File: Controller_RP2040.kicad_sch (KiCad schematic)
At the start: 11 parts, among them J2 Conn_ARM_SWD_TagConnect_TC203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, U3 NCP1117-3.3

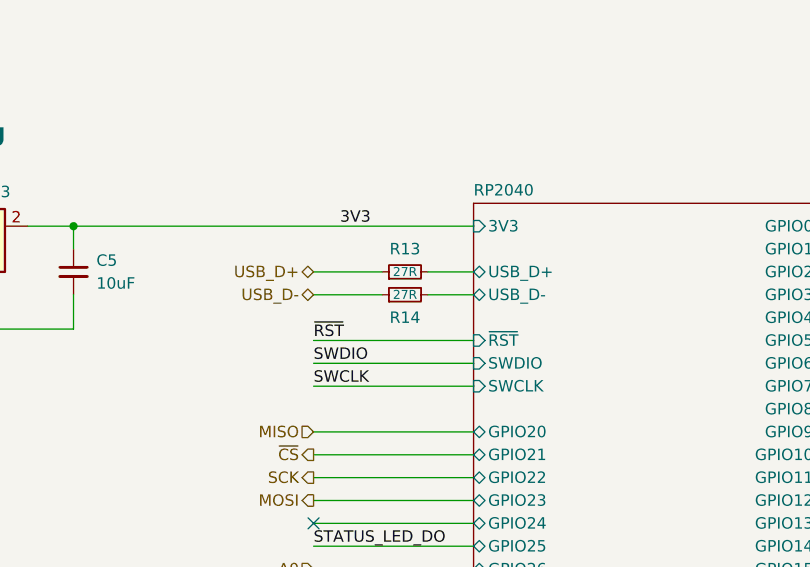
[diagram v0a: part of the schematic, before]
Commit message: Update usb data pins, update to fix 3v3 reg not adj
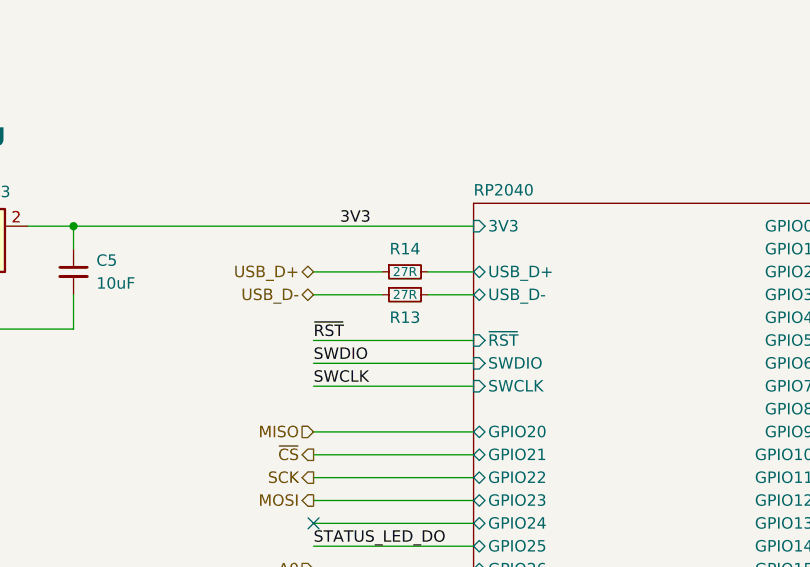
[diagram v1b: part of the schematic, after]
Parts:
- U3: LCSC C233236 -> C146799; MPN NCP1117LPSTADT3G -> NCP1117LPST33T3G; Supplier PN NCP1117LPSTADT3GOSCT-ND -> NCP1117LPST33T3GOSCT-ND
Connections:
- net RP2040/USB_D+: now also R14.2; no longer R13.2
- net RP2040/USB_D-: now also R13.2; no longer R14.2
- net USB_D+: now also R14.1; no longer R13.1
- net USB_D-: now also R13.1; no longer R14.1
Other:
- moved on the sheet: R13, R14
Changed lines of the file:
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@@
 	(symbol
 		(lib_id "Device:R_Small")
-		(at 107.95 67.31 90)
+		(at 107.95 64.77 90)
+		(mirror x)
 		(unit 1)
 		(exclude_from_sim no)
@@
 		(dnp no)
 		(property "Reference" "R14"
-			(at 107.95 69.85 90)
+			(at 107.95 62.23 90)
 			(effects
 				(font
@@
 		)
 		(property "Value" "27R"
-			(at 107.95 67.31 90)
+			(at 107.95 64.77 90)
 			(effects
 				(font
@@
 		)
 		(property "Footprint" "Resistor_SMD:R_0402_1005Metric"
-			(at 107.95 67.31 0)
+			(at 107.95 64.77 0)
 			(effects
 				(font
@@
 		)
 		(property "Datasheet" "https://www.yageo.com/upload/media/product/products/datasheet/rchip/PYu-RC_Group_51_RoHS_L_12.pdf"
-			(at 107.95 67.31 0)
+			(at 107.95 64.77 0)
 			(effects
 				(font
@@
 		)
 		(property "Description" "27 Ohms ±1% 0.063W, 1/16W Chip Resistor 0402 (1005 Metric) Moisture Resistant Thick Film"
-			(at 107.95 67.31 0)
+			(at 107.95 64.77 0)
 			(effects
 				(font
@@
 		)
 		(property "MPN" "RC0402FR-0727RL"
-			(at 107.95 67.31 0)
+			(at 107.95 64.77 0)
 			(effects
 				(font
@@
 		)
 		(property "Manufacturer" "YAGEO"
-			(at 107.95 67.31 0)
+			(at 107.95 64.77 0)
 			(effects
 				(font
@@
 		)
 		(property "Price" "$0.16"
-			(at 107.95 67.31 0)
+			(at 107.95 64.77 0)
 			(effects
 				(font
@@
 		)
 		(property "Rating" "RES 27 OHM 1%  1/16W 0402"
-			(at 107.95 67.31 0)
+			(at 107.95 64.77 0)
 			(effects
 				(font
@@
 		)
 		(property "Supplier" "Digikey"
-			(at 107.95 67.31 0)
+			(at 107.95 64.77 0)
 			(effects
 				(font
@@
 		)
 		(property "Supplier PN" "YAG3086CT-ND"
-			(at 107.95 67.31 0)
+			(at 107.95 64.77 0)
 			(effects
 				(font
@@
 		)
 		(property "Interface" ""
-			(at 107.95 67.31 0)
+			(at 107.95 64.77 0)
 			(effects
 				(font
@@
 		)
 		(property "Substitute" ""
-			(at 107.95 67.31 0)
+			(at 107.95 64.77 0)
 			(effects
 				(font
@@
 		)
 		(property "LCSC" "C138021"
-			(at 107.95 67.31 0)
+			(at 107.95 64.77 0)
 			(effects
 				(font
@@
 			)
 		)
-		(property "Supplier PN" "NCP1117LPSTADT3GOSCT-ND"
+		(property "Supplier PN" "NCP1117LPST33T3GOSCT-ND"
 			(at 58.42 59.69 0)
 			(effects
@@
 			)
 		)
-		(property "MPN" "NCP1117LPSTADT3G"
+		(property "MPN" "NCP1117LPST33T3G"
 			(at 58.42 59.69 0)
 			(effects
@@
 			)
 		)
-		(property "LCSC" "C233236"
+		(property "LCSC" "C146799"
 			(at 58.42 59.69 0)
 			(effects
@@
 	(symbol
 		(lib_id "Device:R_Small")
-		(at 107.95 64.77 90)
+		(at 107.95 67.31 90)
+		(mirror x)
 		(unit 1)
 		(exclude_from_sim no)
@@
 		(dnp no)
 		(property "Reference" "R13"
-			(at 107.95 62.23 90)
+			(at 107.95 69.85 90)
 			(effects
 				(font
@@
 		)
 		(property "Value" "27R"
-			(at 107.95 64.77 90)
+			(at 107.95 67.31 90)
 			(effects
 				(font
@@
 		)
 		(property "Footprint" "Resistor_SMD:R_0402_1005Metric"
-			(at 107.95 64.77 0)
+			(at 107.95 67.31 0)
 			(effects
 				(font
@@
 		)
 		(property "Datasheet" "https://www.yageo.com/upload/media/product/products/datasheet/rchip/PYu-RC_Group_51_RoHS_L_12.pdf"
-			(at 107.95 64.77 0)
+			(at 107.95 67.31 0)
 			(effects
 				(font
@@
 		)
 		(property "Description" "27 Ohms ±1% 0.063W, 1/16W Chip Resistor 0402 (1005 Metric) Moisture Resistant Thick Film"
-			(at 107.95 64.77 0)
+			(at 107.95 67.31 0)
 			(effects
 				(font
@@
 		)
 		(property "MPN" "RC0402FR-0727RL"
-			(at 107.95 64.77 0)
+			(at 107.95 67.31 0)
 			(effects
 				(font
@@
 		)
 		(property "Manufacturer" "YAGEO"
-			(at 107.95 64.77 0)
+			(at 107.95 67.31 0)
 			(effects
 				(font
@@
 		)
 		(property "Price" "$0.16"
-			(at 107.95 64.77 0)
+			(at 107.95 67.31 0)
 			(effects
 				(font
@@
 		)
 		(property "Rating" "RES 27 OHM 1%  1/16W 0402"
-			(at 107.95 64.77 0)
+			(at 107.95 67.31 0)
 			(effects
 				(font
@@
 		)
 		(property "Supplier" "Digikey"
-			(at 107.95 64.77 0)
+			(at 107.95 67.31 0)
 			(effects
 				(font
@@
 		)
 		(property "Supplier PN" "YAG3086CT-ND"
-			(at 107.95 64.77 0)
+			(at 107.95 67.31 0)
 			(effects
 				(font
@@
 		)
 		(property "Interface" ""
-			(at 107.95 64.77 0)
+			(at 107.95 67.31 0)
 			(effects
 				(font
@@
 		)
 		(property "Substitute" ""
-			(at 107.95 64.77 0)
+			(at 107.95 67.31 0)
 			(effects
 				(font
@@
 		)
 		(property "LCSC" "C138021"
-			(at 107.95 64.77 0)
-			(effects
-				(font
+			(at 107.95 67.31 0)
+			(effects
+				(font

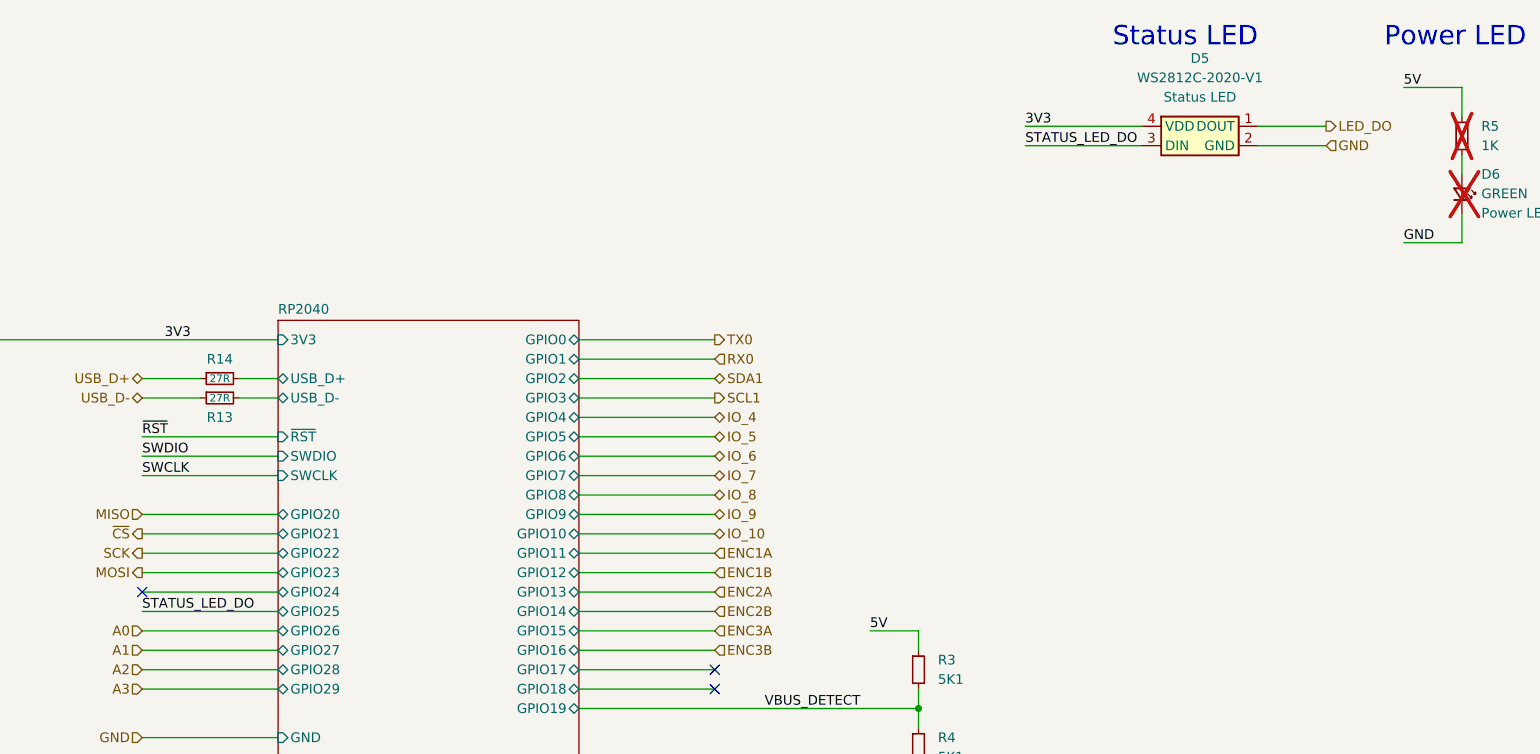
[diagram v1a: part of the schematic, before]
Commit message: Update footprint on back light SK6812MINI LED, add more back lights.
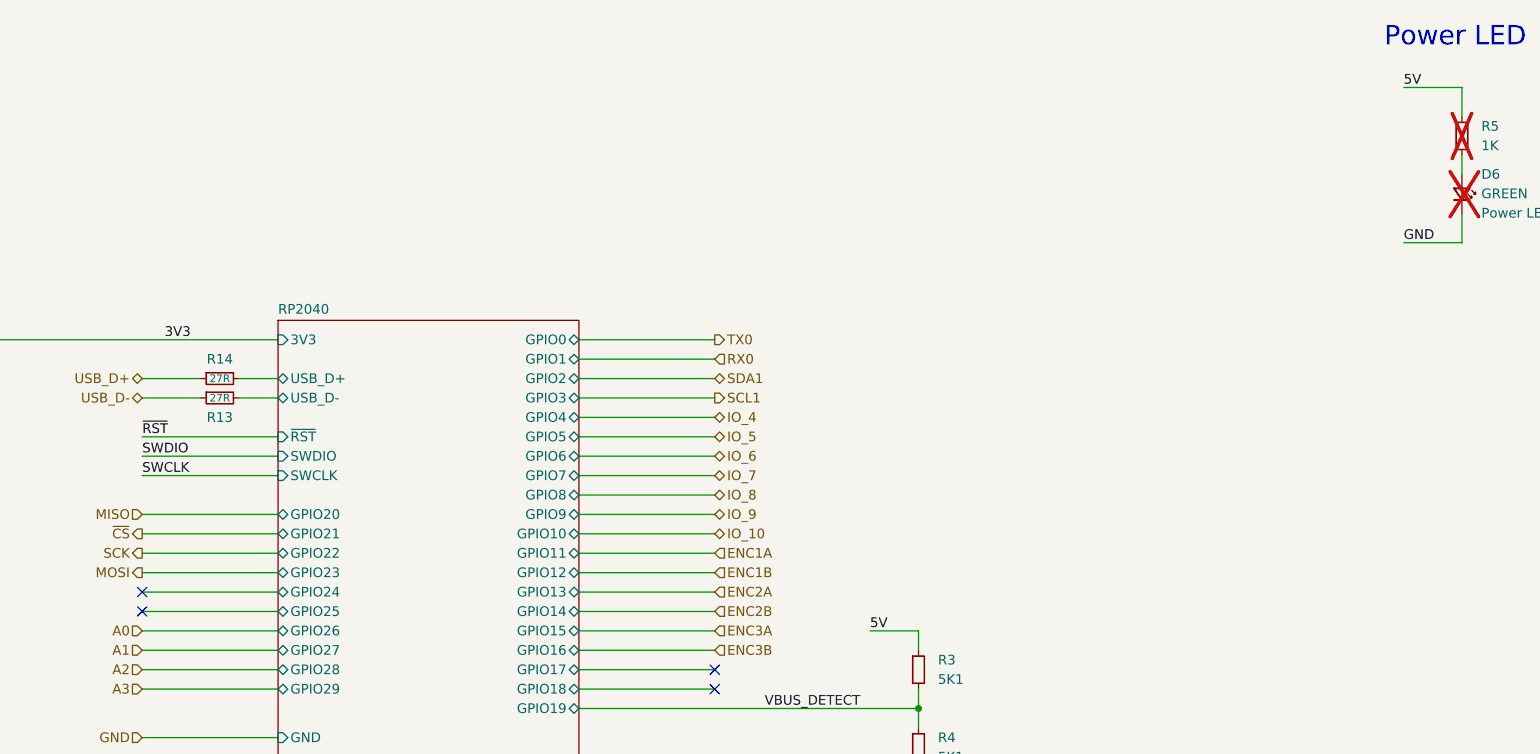
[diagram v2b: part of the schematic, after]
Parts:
- removed D5: WS2812C-2020-V1, Mad_Footprints:WS2812C-2020, symbol Mad_Symbols:WS2812
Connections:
- no-connect marks 4 -> 5
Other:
- note removed: "Status LED"

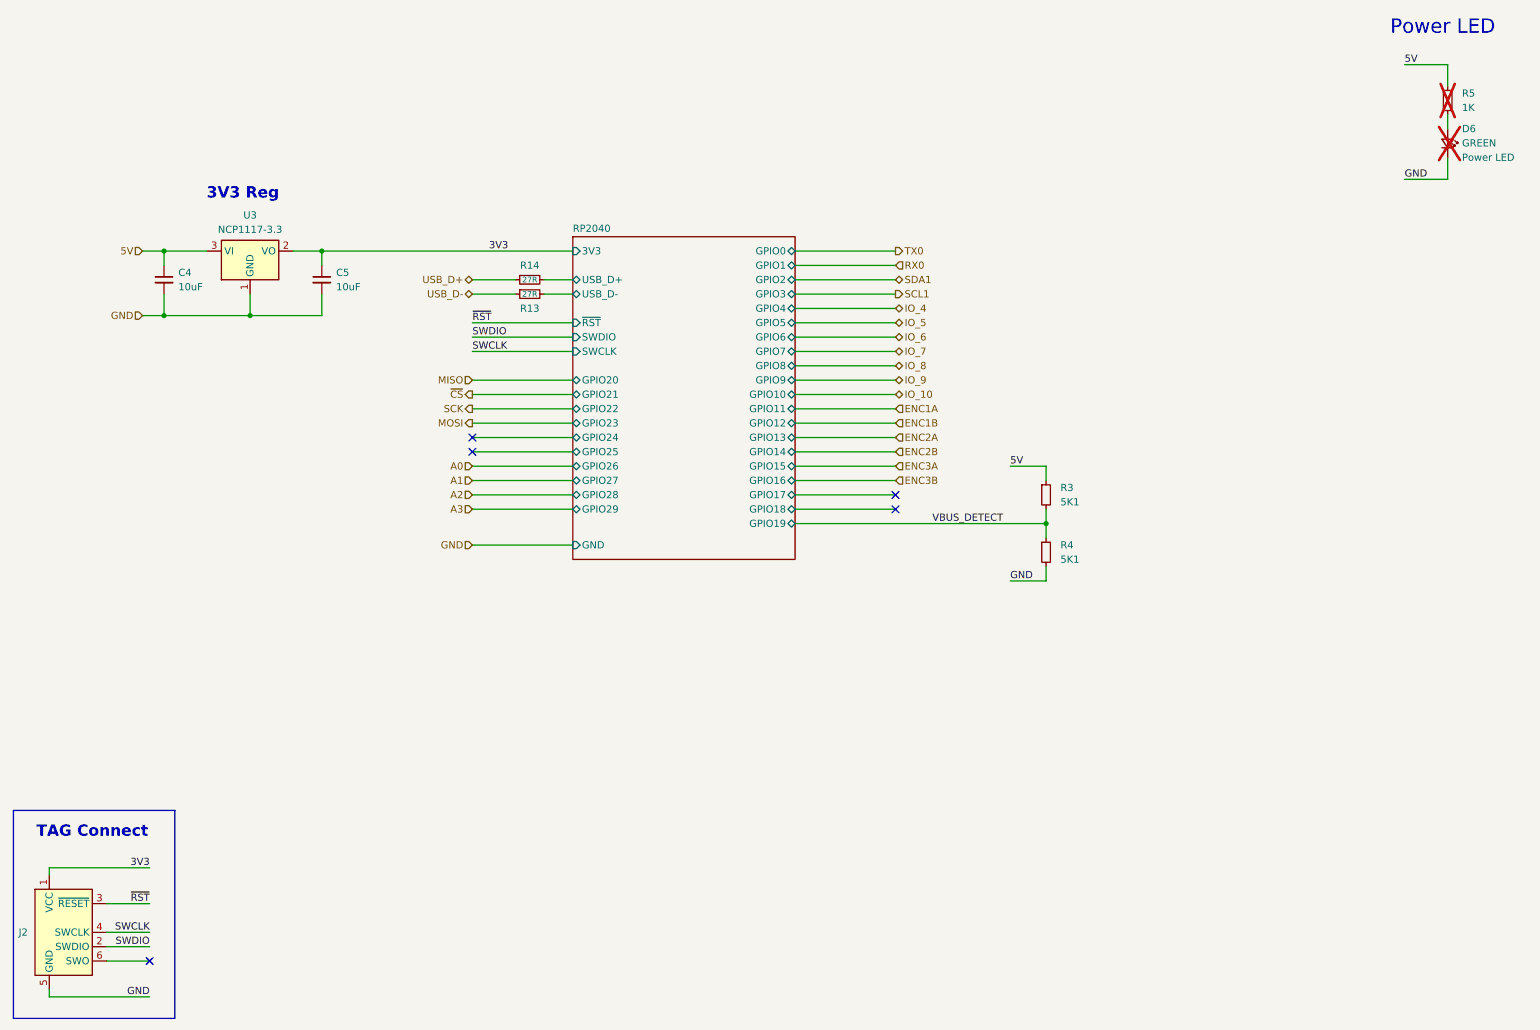
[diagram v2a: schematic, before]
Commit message: Expand board to 4x5, update rev to b
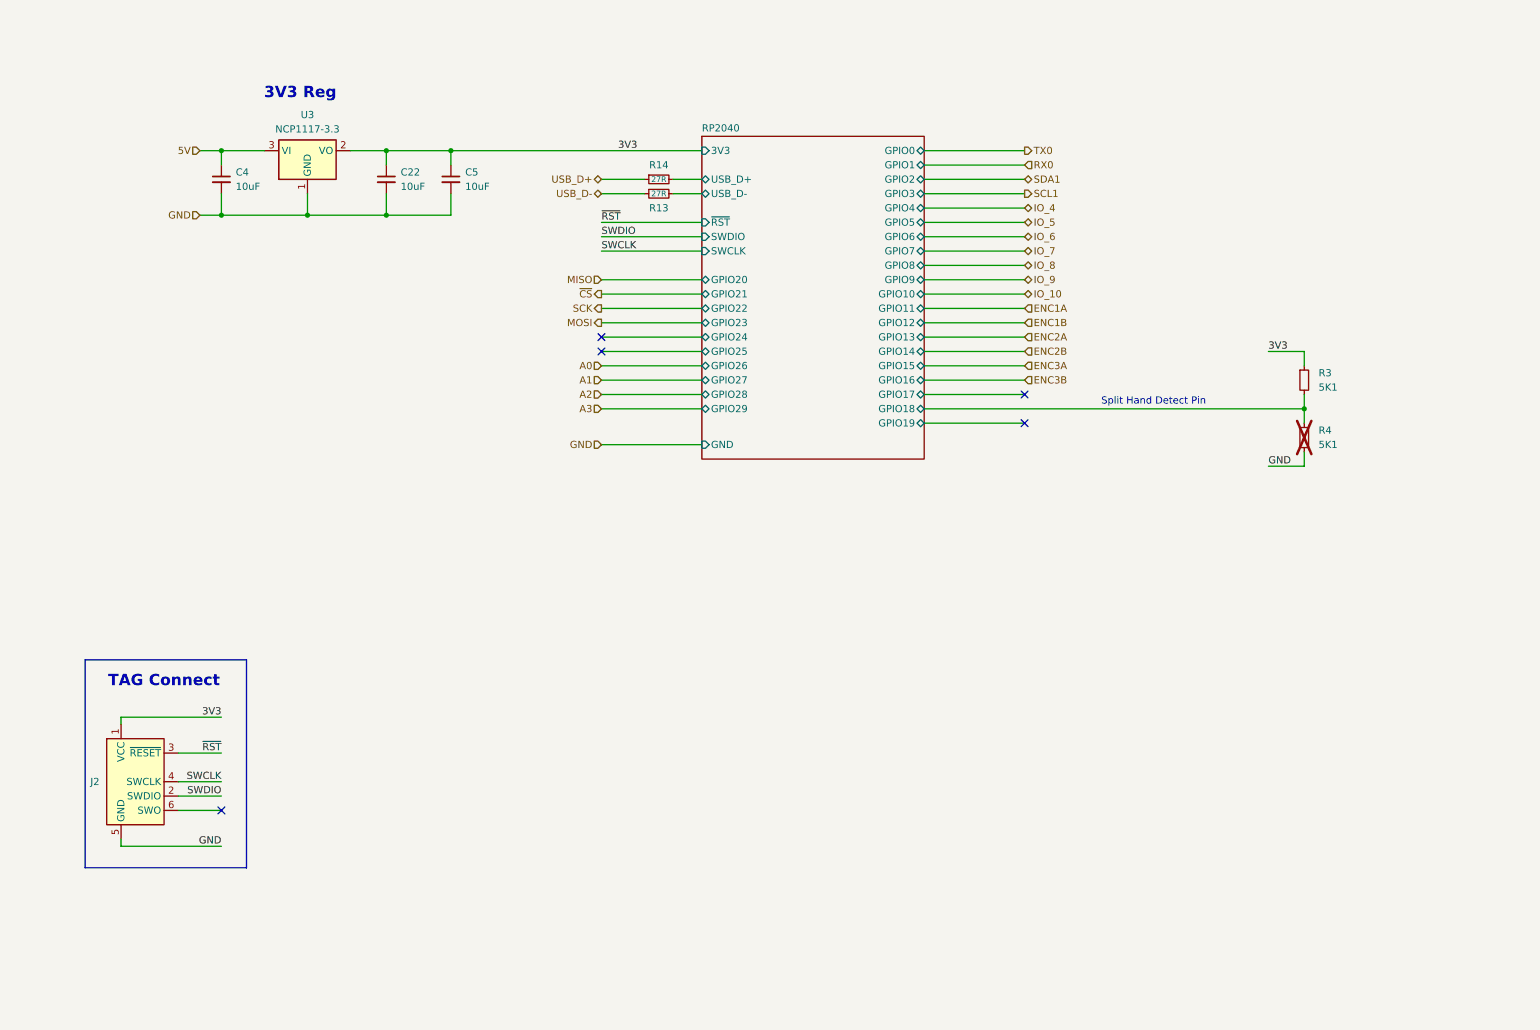
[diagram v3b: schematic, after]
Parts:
- removed D6: GREEN, LED_SMD:LED_0603_1608Metric, symbol Device:LED_Small
- removed R5: 1K, Resistor_SMD:R_0402_1005Metric, symbol Device:R_Small
- added C22: 10uF, Capacitor_SMD:C_0805_2012Metric, symbol Device:C_Small
- R4: now not fitted
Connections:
- net VBUS_DETECT is gone; now on net RP2040/GPIO18: R3.2, R4.1
- net 3V3: now also R3.1, C22.1
- net 5V: no longer R3.1
- net GND: now also C22.2
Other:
- note added: "Split Hand Detect Pin"
- note removed: "Power LED"
- moved on the sheet: C4, C5, J2, R13, R14, R3, U3

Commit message: More placement, start routing, fix up some schematic connections
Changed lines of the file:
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@@
 		)
 	)
-	(hierarchical_label "ENC3B"
+	(hierarchical_label "ENC2B"
 		(shape input)
 		(at 195.58 82.55 0)
@@
 			)
 			(justify right)
-		)
-	)
-	(hierarchical_label "ENC1B"
-		(shape input)
-		(at 195.58 72.39 0)
-		(effects
-			(font
-				(size 1.27 1.27)
-			)
-			(justify left)
 		)
 	)
@@
 		)
 	)
-	(hierarchical_label "ENC2A"
+	(hierarchical_label "ENC1A"
 		(shape input)
 		(at 195.58 74.93 0)
@@
 		)
 	)
-	(hierarchical_label "ENC1A"
-		(shape input)
-		(at 195.58 69.85 0)
-		(effects
-			(font
-				(size 1.27 1.27)
-			)
-			(justify left)
-		)
-	)
-	(hierarchical_label "ENC3A"
+	(hierarchical_label "ENC2A"
 		(shape input)
 		(at 195.58 80.01 0)
@@
 		)
 	)
-	(hierarchical_label "ENC2B"
+	(hierarchical_label "IO_11"
+		(shape bidirectional)
+		(at 195.58 69.85 0)
+		(effects
+			(font
+				(size 1.27 1.27)
+			)
+			(justify left)
+		)
+	)
+	(hierarchical_label "ENC1B"
 		(shape input)
 		(at 195.58 77.47 0)
 		(effects
 			(font
+				(size 1.27 1.27)
+			)
+			(justify left)
+		)
+	)
+	(hierarchical_label "IO_12"
+		(shape bidirectional)
+		(at 195.58 72.39 0)
+		(effects
+			(font
